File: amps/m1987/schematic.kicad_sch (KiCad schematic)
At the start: 75 parts, among them T1 OT

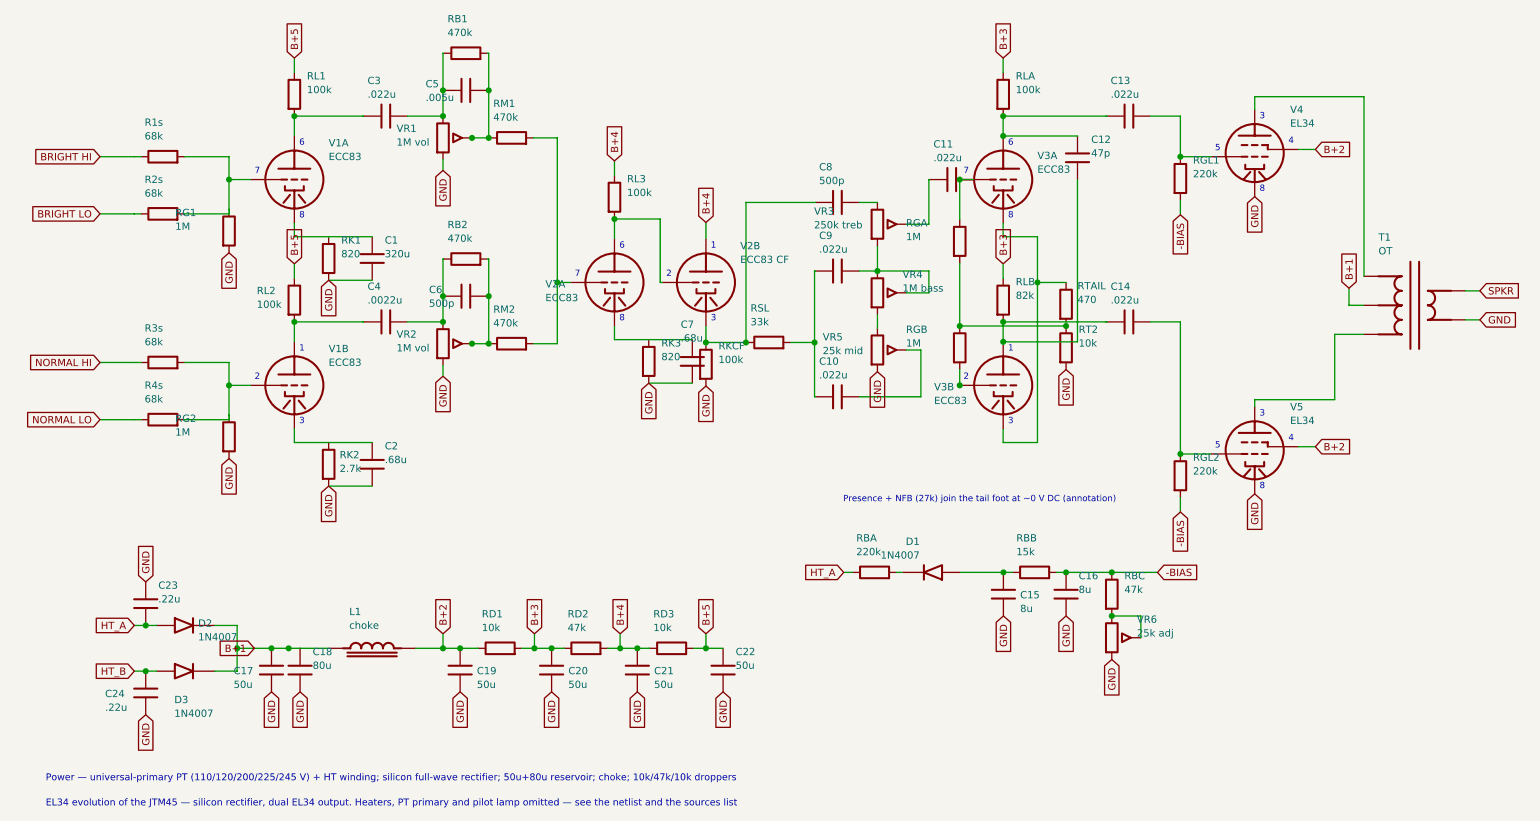
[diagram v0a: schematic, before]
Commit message: Correct M1987 rail droppers and draw source feedback network
Read 1987u.gif at native2023x1304, crops(910,190)-(1610,670) and(1760,170)-(1990,490). The screen-to-PI chain has two10k/1W resistors, then10k to V2 and10k to V1. The47k(100k) is feedback from8 ohms, not a rail dropper. Represent the first pair as the disclosed RD1 20k2W equivalent; restore RD2 10k.

Draw the47k feedback,5k grounded presence track and both .1u caps; separate the tail foot from the grid-leak junction in model,sheet and derived board. Both board styles,OG and schematic preview inspected; zero collision lint. No voltage chart or verification claim invented. Source: https://www.drtube.com/schematics/marshall/1987u.gif

Signed-off-by: AnalogMaker <theanalogmaker@gmail.com>
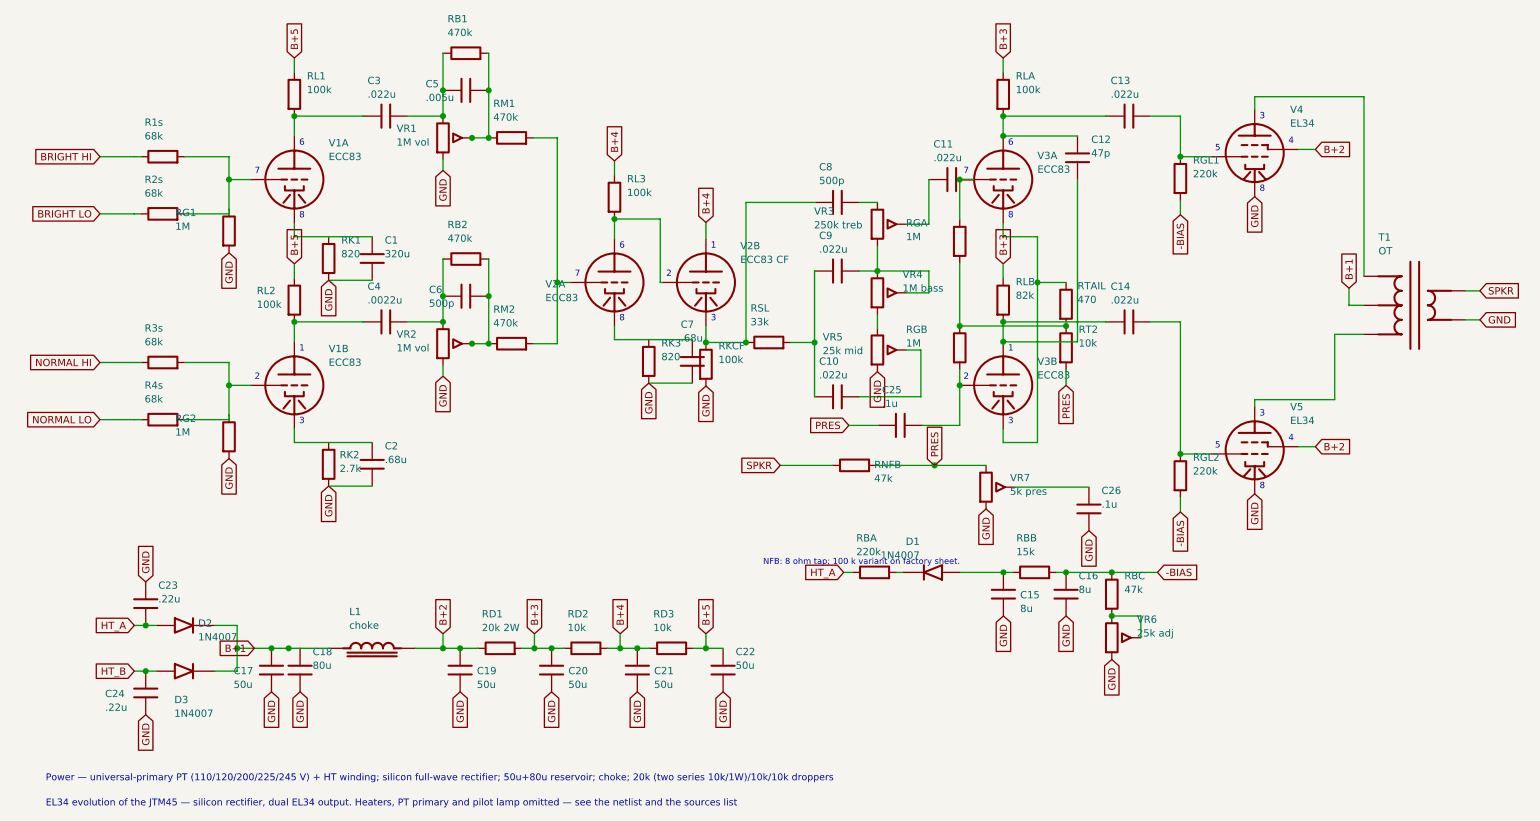
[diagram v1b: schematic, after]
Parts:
- removed C21: 50u, symbol cx:C
- removed RBA: 220k, symbol cx:R
- removed RD2: 47k, symbol cx:R
- removed RD3: 10k, symbol cx:R
- removed T1: OT, symbol cx:OT_PP
- removed V4: EL34, symbol cx:PENTODE
- added C15: 8u, symbol cx:C
- added C19, C22: 50u, symbol cx:C
- added C25, C26: .1u, symbol cx:C
- added RBB: 15k, symbol cx:R
- added RBC, RNFB: 47k, symbol cx:R
- added RGL2: 220k, symbol cx:R
- added VR7: 5k pres, symbol cx:POT
- C21: renamed from C15; value 8u -> 50u
- D2: renamed from C17; value 50u -> 1N4007; symbol cx:C -> cx:DIODE_SS
- RBA: renamed from RBC; value 47k -> 220k
- RD1: value 10k -> 20k 2W
- RD2: renamed from C22; value 50u -> 10k; symbol cx:C -> cx:R
- RD3: renamed from RBB; value 15k -> 10k
- T1: renamed from D2; value 1N4007 -> OT; symbol cx:DIODE_SS -> cx:OT_PP
- V4: renamed from RGL2; value 220k -> EL34; symbol cx:R -> cx:PENTODE
- renumbered C19 to C17
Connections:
- net -BIAS: now also RBB.2, RBC.1, RGL2.2; no longer RBA.1, RD3.2, V4.2
- net B+1: now also C17.1, D2.2 (K); no longer D2.1
- net B+2: now also V4.3 (G2), C19.1; no longer C17.1
- net B+3: now also RD2.1
- net B+4: now also C21.1, RD2.2, RD3.1
- net B+5: now also RD3.2, C22.1; no longer RD2.1
- net GND: now also T1.5 (SEC_C), V4.4 (K), C15.2, C19.2, C22.2, C26.2, VR7.3; no longer D2.2, RD2.2, RT2.2
- net HT_A: now also D2.1 (A), RBA.1; no longer T1.1 (A)
- net SPKR: now also T1.4 (SEC_H), RNFB.1
- net at D1.2 (K): now also RBA.2
- net at VR6.1, VR6.2 (W): now also RBC.2; no longer RBA.2
- net at RGB.2, V3B.2 (G): now also C25.2
- net at C13.2, RGL1.1: now also V4.2 (G1)
- net at V5.1 (P): now also T1.3 (PRI_B)
- net at C14.2, V5.2 (G1): now also RGL2.1; no longer V4.1
- new net: C15.1, D1.1 (A), RBB.1
- new net: T1.1 (PRI_A), V4.1 (P)
- new net: C26.1, VR7.2 (W)
- new net PRES: C25.1, RNFB.2, RT2.2, VR7.1
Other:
- note added: "NFB: 8 ohm tap; 100 k variant on factory sheet."
- note added: "Power — universal-primary PT (110/120/200/225/245 V) + HT winding; silicon full-wave rectifier; 50u+80u reservoir; choke; 20k (two series 10k/1W)/10k/10k droppers"
- note removed: "Power — universal-primary PT (110/120/200/225/245 V) + HT winding; silicon full-wave rectifier; 50u+80u reservoir; choke; 10k/47k/10k droppers"
- note removed: "Presence + NFB (27k) join the tail foot at ~0 V DC (annotation)"
- moved on the sheet: C17, C21, D2, RBA, RD3
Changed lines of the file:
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@@
   (symbol (lib_id "cx:TRIODE") (at 180.2 77.689 0) (unit 1)
     (in_bom yes) (on_board yes)
-    (property "Reference" "V3B" (at 168.112 77.969 0) (effects (font (size 1.27 1.27)) (justify left)))
-    (property "Value" "ECC83" (at 168.112 80.369 0) (effects (font (size 1.27 1.27)) (justify left))))
+    (property "Reference" "V3B" (at 186.18 73.509 0) (effects (font (size 1.27 1.27)) (justify left)))
+    (property "Value" "ECC83" (at 186.18 75.909 0) (effects (font (size 1.27 1.27)) (justify left))))
   (wire (pts (xy 180.2 34.069) (xy 180.2 30.589))
     (stroke (width 0) (type default)))
@@
     (property "Reference" "RT2" (at 193.4 67.919 0) (effects (font (size 1.27 1.27)) (justify left)))
     (property "Value" "10k" (at 193.4 70.319 0) (effects (font (size 1.27 1.27)) (justify left))))
-  (global_label "GND" (shape input) (at 191.2 74.929 270)
+  (wire (pts (xy 191.2 74.929) (xy 191.2 77.689))
+    (stroke (width 0) (type default)))
+  (global_label "PRES" (shape input) (at 191.2 77.689 270)
     (effects (font (size 1.27 1.27)) (justify right)))
   (wire (pts (xy 172.6 41.689) (xy 172.6 48.689))
@@
     (property "Reference" "RGB" (at 163.2 67.919 0) (effects (font (size 1.27 1.27)) (justify left)))
     (property "Value" "1M" (at 163.2 70.319 0) (effects (font (size 1.27 1.27)) (justify left))))
-  (text "Presence + NFB (27k) join the tail foot at ~0 V DC (annotation)" (at 152.2 97.689 0)
-    (effects (font (size 1.1 1.1)) (justify left)))
+  (symbol (lib_id "cx:C") (at 162.2 84.689 90) (unit 1)
+    (in_bom yes) (on_board yes)
+    (property "Reference" "C25" (at 159 78.489 270) (effects (font (size 1.27 1.27)) (justify left)))
+    (property "Value" ".1u" (at 159 80.889 270) (effects (font (size 1.27 1.27)) (justify left))))
+  (wire (pts (xy 166.01 84.689) (xy 172.6 84.689))
+    (stroke (width 0) (type default)))
+  (wire (pts (xy 172.6 84.689) (xy 172.6 77.689))
+    (stroke (width 0) (type default)))
+  (wire (pts (xy 158.39 84.689) (xy 153.2 84.689))
+    (stroke (width 0) (type default)))
+  (global_label "PRES" (shape input) (at 153.2 84.689 180)
+    (effects (font (size 1.27 1.27)) (justify right)))
+  (global_label "SPKR" (shape input) (at 141.2 91.689 180)
+    (effects (font (size 1.27 1.27)) (justify right)))
+  (wire (pts (xy 141.2 91.689) (xy 150.39 91.689))
+    (stroke (width 0) (type default)))
+  (symbol (lib_id "cx:R") (at 154.2 91.689 90) (unit 1)
+    (in_bom yes) (on_board yes)
+    (property "Reference" "RNFB" (at 157.64 91.573 270) (effects (font (size 1.27 1.27)) (justify left)))
+    (property "Value" "47k" (at 157.64 93.973 270) (effects (font (size 1.27 1.27)) (justify left))))
+  (wire (pts (xy 158.01 91.689) (xy 168.2 91.689))
+    (stroke (width 0) (type default)))
+  (wire (pts (xy 168.2 91.689) (xy 177.2 91.689))
+    (stroke (width 0) (type default)))
+  (junction (at 168.2 91.689) (diameter 1.056) (color 0 0 0 0))
+  (global_label "PRES" (shape input) (at 168.2 91.689 90)
+    (effects (font (size 1.27 1.27)) (justify left)))
+  (symbol (lib_id "cx:POT") (at 177.2 95.499 0) (unit 1)
+    (in_bom yes) (on_board yes)
+    (property "Reference" "VR7" (at 181.402 93.859 0) (effects (font (size 1.27 1.27)) (justify left)))
+    (property "Value" "5k pres" (at 181.402 96.259 0) (effects (font (size 1.27 1.27)) (justify left))))
+  (global_label "GND" (shape input) (at 177.2 99.309 270)
+    (effects (font (size 1.27 1.27)) (justify right)))
+  (wire (pts (xy 182.28 95.499) (xy 195.2 95.499))
+    (stroke (width 0) (type default)))
+  (symbol (lib_id "cx:C") (at 195.2 99.309 0) (unit 1)
+    (in_bom yes) (on_board yes)
+    (property "Reference" "C26" (at 197.4 96.109 0) (effects (font (size 1.27 1.27)) (justify left)))
+    (property "Value" ".1u" (at 197.4 98.509 0) (effects (font (size 1.27 1.27)) (justify left))))
+  (global_label "GND" (shape input) (at 195.2 103.119 270)
+    (effects (font (size 1.27 1.27)) (justify right)))
+  (text "NFB: 8 ohm tap; 100 k variant on factory sheet." (at 138.2 108.689 0)
+    (effects (font (size 1.05 1.05)) (justify left)))
   (wire (pts (xy 180.2 30.589) (xy 198.2 30.589))
     (stroke (width 0) (type default)))
@@
     (in_bom yes) (on_board yes)
     (property "Reference" "RD1" (at 88.9996 117.689 270) (effects (font (size 1.27 1.27)) (justify left)))
-    (property "Value" "10k" (at 88.9996 120.089 270) (effects (font (size 1.27 1.27)) (justify left))))
+    (property "Value" "20k 2W" (at 88.9996 120.089 270) (effects (font (size 1.27 1.27)) (justify left))))
   (wire (pts (xy 88.1996 123.689) (xy 88.3896 123.689))
     (stroke (width 0) (type default)))
@@
     (in_bom yes) (on_board yes)
     (property "Reference" "RD2" (at 104 117.689 270) (effects (font (size 1.27 1.27)) (justify left)))
-    (property "Value" "47k" (at 104 120.089 270) (effects (font (size 1.27 1.27)) (justify left))))
+    (property "Value" "10k" (at 104 120.089 270) (effects (font (size 1.27 1.27)) (justify left))))
   (wire (pts (xy 103.2 123.689) (xy 103.39 123.689))
     (stroke (width 0) (type default)))
@@
   (text "8" (at 225.05 95.404 0)
     (effects (font (size 1.1 1.1)) (justify left)))
-  (text "Power — universal-primary PT (110/120/200/225/245 V) + HT winding; silicon full-wave rectifier; 50u+80u reservoir; choke; 10k/47k/10k droppers" (at 12.7 146.467 0)
+  (text "Power — universal-primary PT (110/120/200/225/245 V) + HT winding; silicon full-wave rectifier; 50u+80u reservoir; choke; 20k (two series 10k/1W)/10k/10k droppers" (at 12.7 146.467 0)
     (effects (font (size 1.2 1.2)) (justify left)))
   (text "EL34 evolution of the JTM45 — silicon rectifier, dual EL34 output. Heaters, PT primary and pilot lamp omitted — see the netlist and the sources list" (at 12.7 150.867 0)

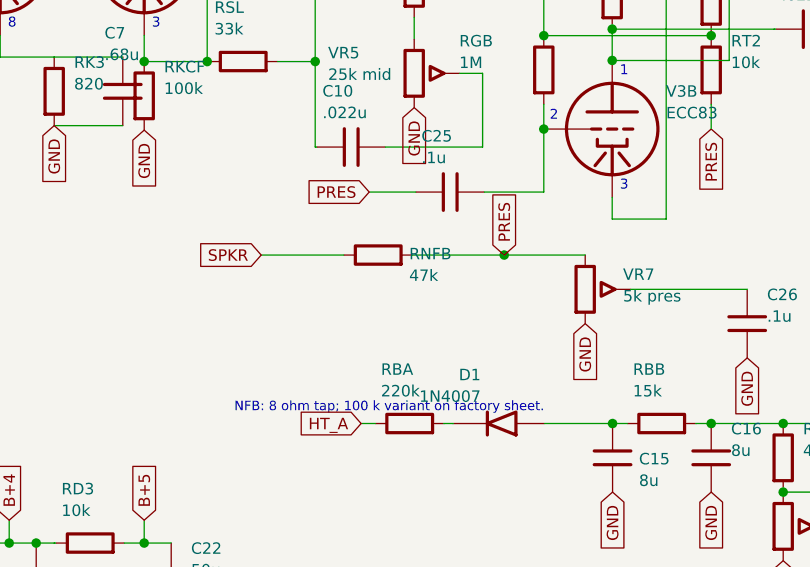
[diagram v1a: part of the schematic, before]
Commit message: Correct JTM45 presence capacitor and clear M1987 feedback label
Read the JTM45 wiper capacitor as 0.1 uF from the native factory sheet, correcting the inherited 0.01 uF annotation. Keep its BOM, chassis exclusion and source notes consistent. Move the M1987 RNFB properties below their resistor after actual KiCanvas review showed the reference crossing the outgoing wire.

Signed-off-by: AnalogMaker <theanalogmaker@gmail.com>
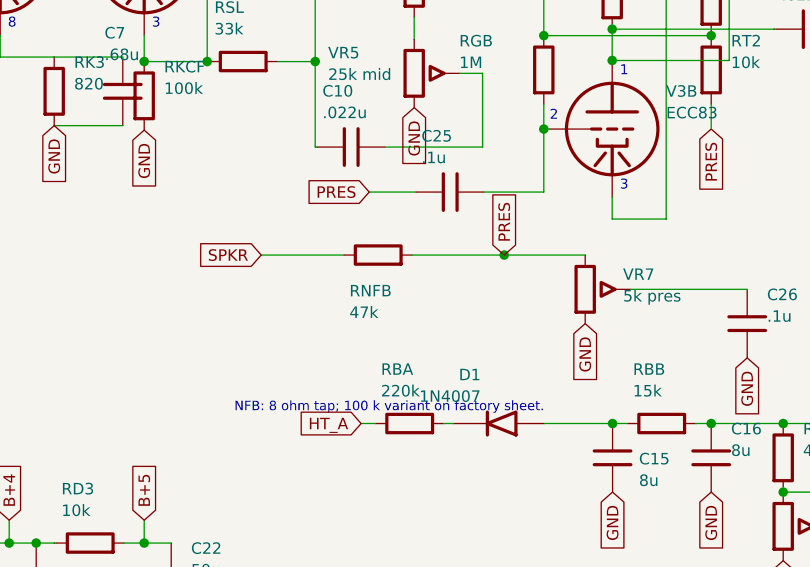
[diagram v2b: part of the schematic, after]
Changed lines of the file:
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@@
   (symbol (lib_id "cx:R") (at 154.2 91.689 90) (unit 1)
     (in_bom yes) (on_board yes)
-    (property "Reference" "RNFB" (at 157.64 91.573 270) (effects (font (size 1.27 1.27)) (justify left)))
-    (property "Value" "47k" (at 157.64 93.973 270) (effects (font (size 1.27 1.27)) (justify left))))
+    (property "Reference" "RNFB" (at 151 95.689 270) (effects (font (size 1.27 1.27)) (justify left)))
+    (property "Value" "47k" (at 151 98.089 270) (effects (font (size 1.27 1.27)) (justify left))))
   (wire (pts (xy 158.01 91.689) (xy 168.2 91.689))
     (stroke (width 0) (type default)))
